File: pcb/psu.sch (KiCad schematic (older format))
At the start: 46 parts, among them J1 CONN_INTEGRALSTICK_FPGA_DEVICE, J2 CONN_INTEGRALSTICK_MCU_DEVICE, U1 STM32F777NIH6‎, U2 XC7A50T-1FTG256C, U7 LTC3374-QFN

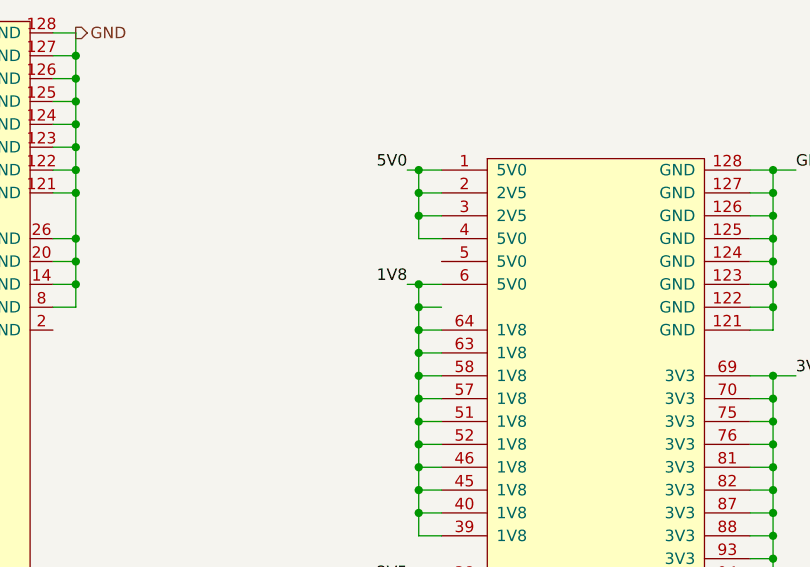
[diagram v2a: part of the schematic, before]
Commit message: Initial layout of LVDS bank
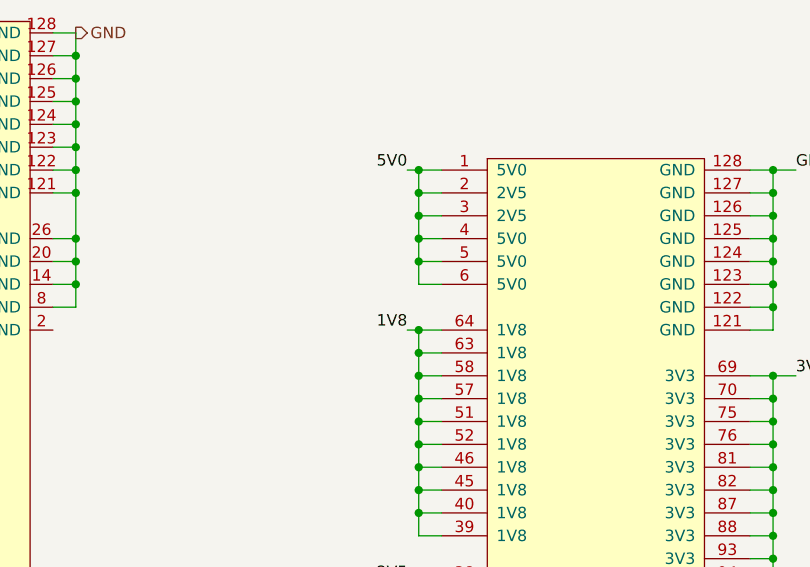
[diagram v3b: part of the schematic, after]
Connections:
- net 1V8: no longer J1.6 (5V0)
- net 5V0: now also J1.5 (5V0), J1.6 (5V0)
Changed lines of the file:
@@
 Connection ~ 4150 8150
 Wire Wire Line
-	4100 8450 4150 8450
-Wire Wire Line
-	4150 8450 4150 8550
-Wire Wire Line
-	4150 8550 4250 8550
-Connection ~ 4150 8450
-Wire Wire Line
-	4150 8450 4250 8450
-Wire Wire Line
-	4150 8550 4150 8650
-Wire Wire Line
-	4150 8650 4250 8650
-Connection ~ 4150 8550
+	4100 8650 4150 8650
 Wire Wire Line
 	4150 8650 4150 8750
@@
 	4150 8750 4250 8750
 Connection ~ 4150 8650
+Wire Wire Line
+	4150 8650 4250 8650
 Wire Wire Line
 	4150 8750 4150 8850
@@
 Text Label 1300 7350 2    50   ~ 0
 3V3
-Text Label 4100 8450 2    50   ~ 0
+Text Label 4100 8650 2    50   ~ 0
 1V8
 Text HLabel 1500 5750 0    50   Output ~ 0
@@
 Wire Wire Line
 	7900 5900 8000 5900
+Wire Wire Line
+	4150 8450 4250 8450
+Connection ~ 4150 8250
+Wire Wire Line
+	4250 8350 4150 8350
+Wire Wire Line
+	4150 8250 4150 8350
+Connection ~ 4150 8350
+Wire Wire Line
+	4150 8350 4150 8450
 $EndSCHEMATC

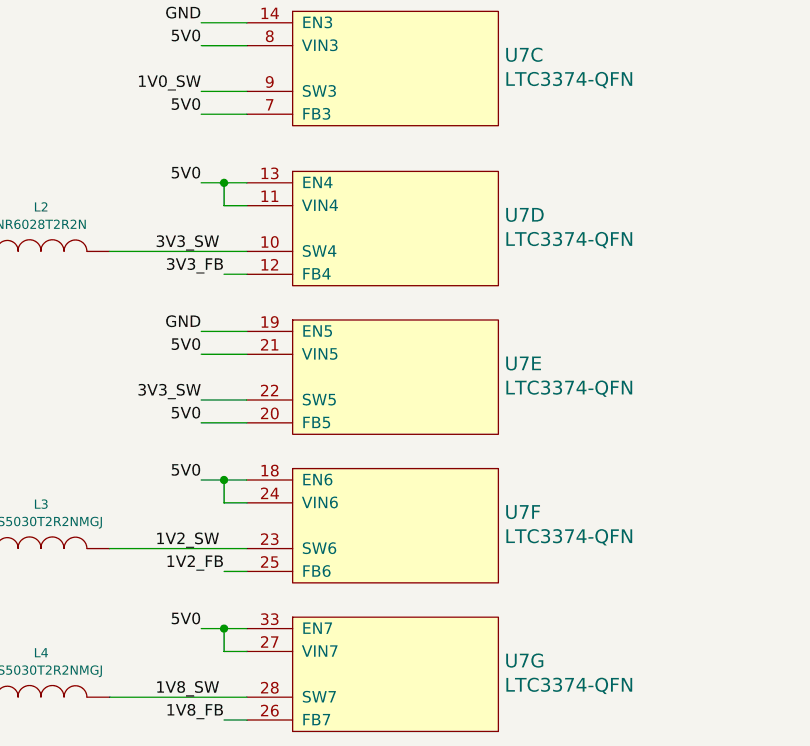
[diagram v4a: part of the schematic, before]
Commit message: Initial placement of SMPS and inductors. No caps.
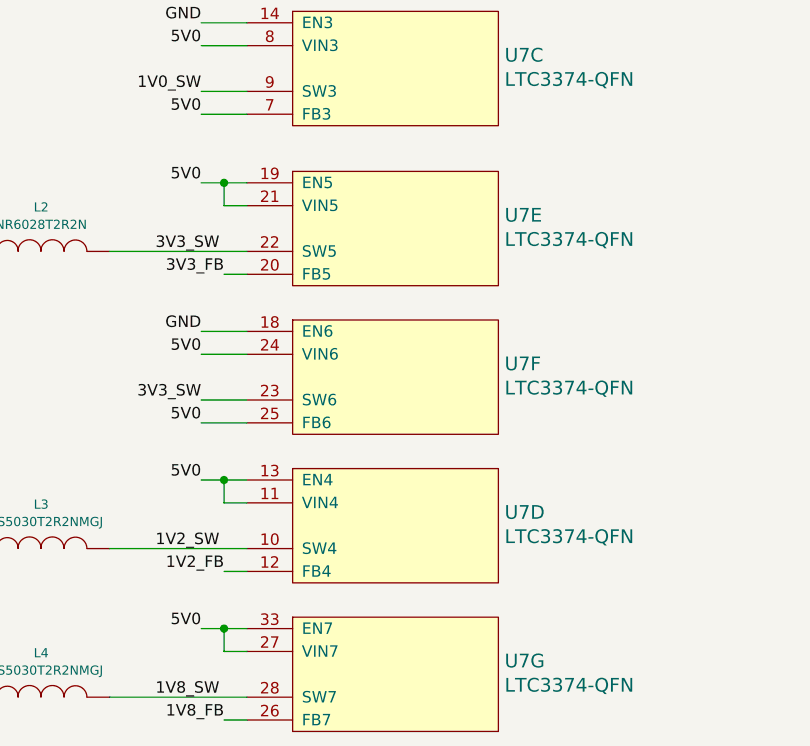
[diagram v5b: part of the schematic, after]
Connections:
- net 1V2_FB: now also U7.12 (FB4); no longer U7.25 (FB6)
- net 1V2_SW: now also U7.10 (SW4); no longer U7.23 (SW6)
- net 3V3_FB: now also U7.20 (FB5); no longer U7.12 (FB4)
- net 3V3_SW: now also U7.23 (SW6); no longer U7.10 (SW4)
- net 5V0: now also U7.19 (EN5), U7.25 (FB6); no longer U7.18 (EN6), U7.20 (FB5)
- net GND: now also U7.18 (EN6); no longer U7.19 (EN5)
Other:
- moved on the sheet: U7D, U7E, U7F
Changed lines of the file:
@@
 L power-azonenberg:LTC3374-QFN U7
 U 4 1 5B828233
+P 2900 4650
+F 0 "U7" H 3827 4958 60  0000 L CNN
+F 1 "LTC3374-QFN" H 3827 4852 60  0000 L CNN
+F 2 "azonenberg_pcb:QFN_38_0.5MM_5x7MM" H 2900 4650 60  0001 C CNN
+F 3 "" H 2900 4650 60  0000 C CNN
+	4    2900 4650
+	1    0    0    -1
+$EndComp
+$Comp
+L power-azonenberg:LTC3374-QFN U7
+U 5 1 5B8282AB
 P 2900 3350
 F 0 "U7" H 3827 3658 60  0000 L CNN
@@
 F 2 "azonenberg_pcb:QFN_38_0.5MM_5x7MM" H 2900 3350 60  0001 C CNN
 F 3 "" H 2900 3350 60  0000 C CNN
-	4    2900 3350
+	5    2900 3350
 	1    0    0    -1
 $EndComp
 $Comp
 L power-azonenberg:LTC3374-QFN U7
-U 5 1 5B8282AB
+U 6 1 5B82834C
 P 2900 4000
 F 0 "U7" H 3827 4308 60  0000 L CNN
@@
 F 2 "azonenberg_pcb:QFN_38_0.5MM_5x7MM" H 2900 4000 60  0001 C CNN
 F 3 "" H 2900 4000 60  0000 C CNN
-	5    2900 4000
+	6    2900 4000
 	1    0    0    -1
 $EndComp
-$Comp
-L power-azonenberg:LTC3374-QFN U7
-U 6 1 5B82834C
-P 2900 4650
-F 0 "U7" H 3827 4958 60  0000 L CNN
-F 1 "LTC3374-QFN" H 3827 4852 60  0000 L CNN
-F 2 "azonenberg_pcb:QFN_38_0.5MM_5x7MM" H 2900 4650 60  0001 C CNN
-F 3 "" H 2900 4650 60  0000 C CNN
-	6    2900 4650
-	1    0    0    -1
-$EndComp

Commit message: Finished initial routing
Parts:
- added TP11: TESTPAD, azonenberg_pcb:TESTPOINT_SMT_0.5MM, symbol conn:CONN_01X01
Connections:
- net GND: now also J2.2 (GND)
- net MCU_VBAT: now also TP11.1 (P1)
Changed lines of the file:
@@
 Sheet 2 8
 Title "INTEGRALSTICK Compute Module"
-Date "2018-11-20"
+Date "2018-11-23"
 Rev "0.1"
 Comp "Andrew D. Zonenberg"
@@
 Wire Wire Line
 	1300 7350 1350 7350
-Wire Wire Line
-	1350 10850 1450 10850
 Connection ~ 1350 7350
 Wire Wire Line
@@
 Wire Wire Line
 	1450 10750 1350 10750
-Connection ~ 1350 10750
-Wire Wire Line
-	1350 10750 1350 10850
 Wire Wire Line
 	1450 10650 1350 10650
@@
 Wire Wire Line
 	4150 8350 4150 8450
+$Comp
+L conn:CONN_01X01 TP?
+U 1 1 5C11F6A8
+P 8650 6550
+AR Path="/5C11F6A8" Ref="TP?"  Part="1"
+AR Path="/5B6B7005/5C11F6A8" Ref="TP11"  Part="1"
+F 0 "TP11" H 8728 6591 50  0000 L CNN
+F 1 "TESTPAD" H 8728 6500 50  0000 L CNN
+F 2 "azonenberg_pcb:TESTPOINT_SMT_0.5MM" H 8650 6550 50  0001 C CNN
+F 3 "" H 8650 6550 50  0001 C CNN
+	1    8650 6550
+	1    0    0    -1
+$EndComp
+Wire Wire Line
+	8450 6550 8000 6550
+Wire Wire Line
+	2650 8550 2650 8650
+Wire Wire Line
+	2650 8650 2550 8650
+Connection ~ 2650 8550
 $EndSCHEMATC
